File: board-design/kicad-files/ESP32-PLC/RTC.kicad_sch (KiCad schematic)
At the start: 17 parts, among them U7 MCP7940N-xSN, U8 24LC512

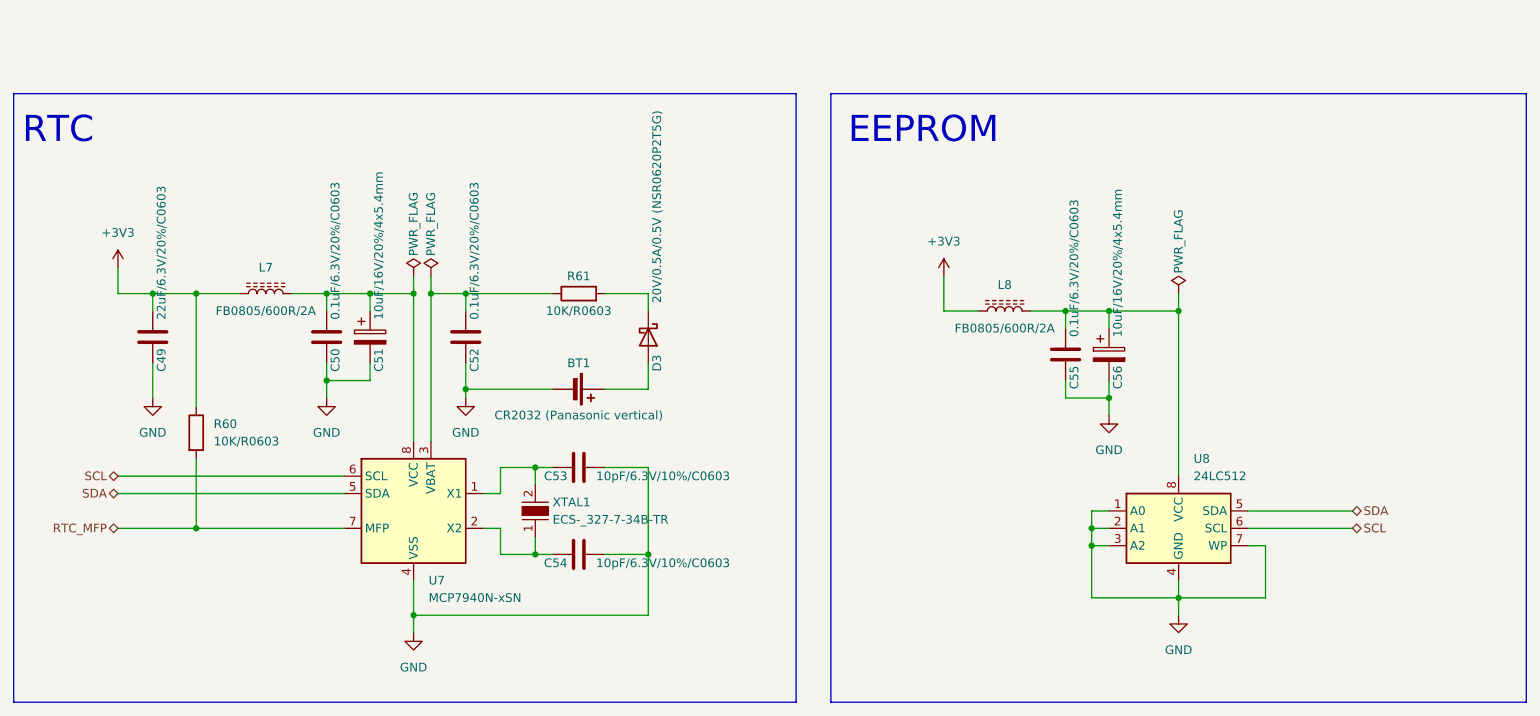
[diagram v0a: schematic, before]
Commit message: [UPDATE]
Finished ESP32-PLC board design

Signed-off-by: Nicolae-Andrei Vasile <vasilenicolaeandrei@gmail.com>
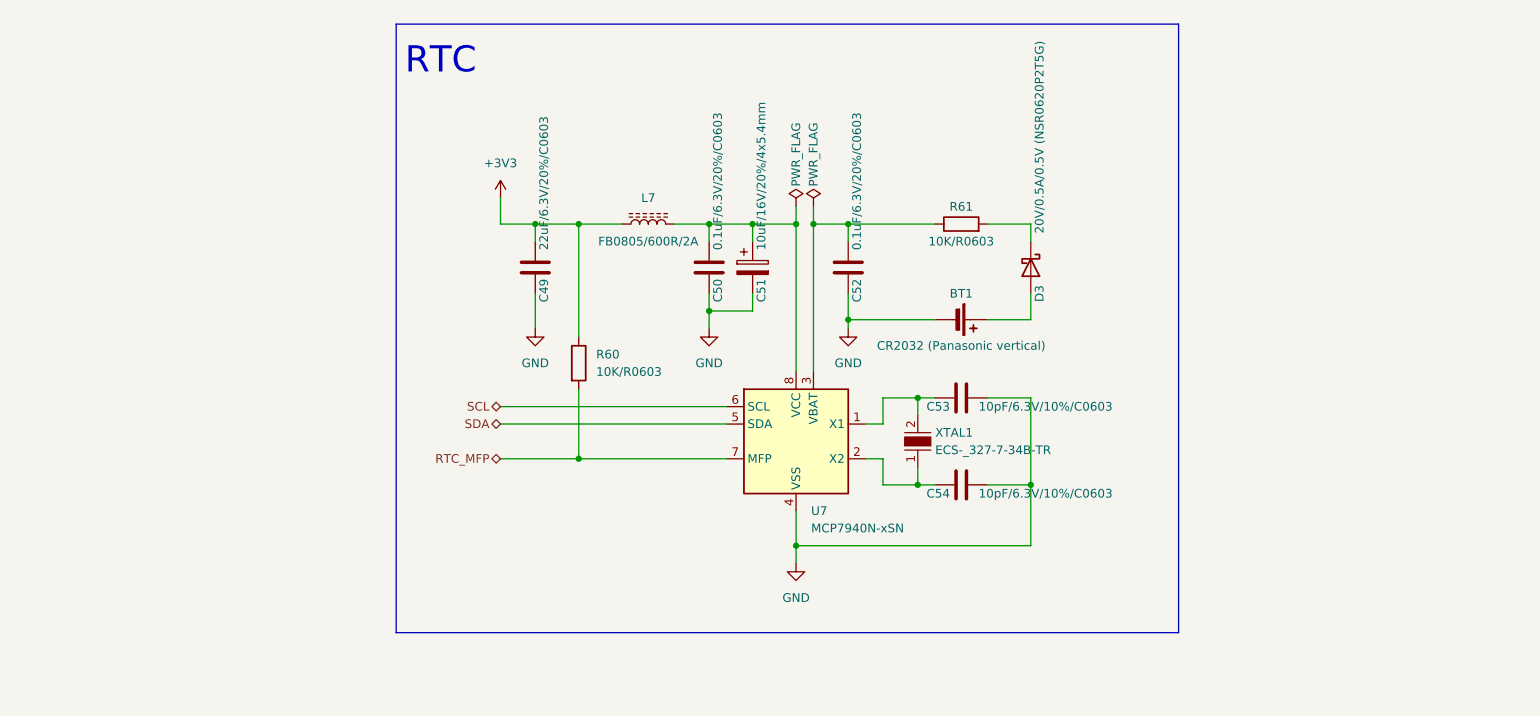
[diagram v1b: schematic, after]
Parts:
- removed C55: 0.1uF/6.3V/20%/C0603, Capacitor_SMD:C_0603_1608Metric, symbol Device:C
- removed C56: 10uF/16V/20%/4x5.4mm, Capacitor_SMD:CP_Elec_4x5.4, symbol Device:C_Polarized
- removed L8: FB0805/600R/2A, Inductor_SMD:L_0805_2012Metric, symbol Device:L_Ferrite
- removed U8: 24LC512, Package_SO:SOIC-8_3.9x4.9mm_P1.27mm, symbol Memory_EEPROM:24LC512
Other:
- note removed: "EEPROM"
- title: (none) -> ESP32
- moved on the sheet: BT1, C49, C50, C51, C52, C53, C54, D3, L7, R60, R61, U7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
